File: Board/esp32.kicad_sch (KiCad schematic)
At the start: 7 parts, among them U1 ESP32-WROOM-32

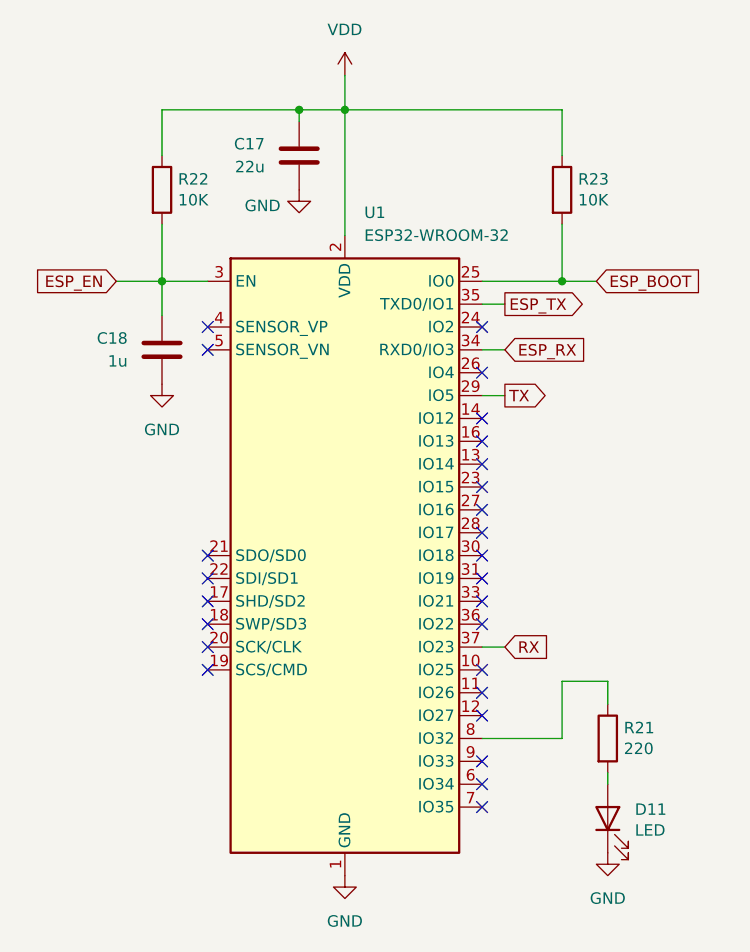
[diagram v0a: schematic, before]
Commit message: Minor fixes and improvements. Changes board shape.
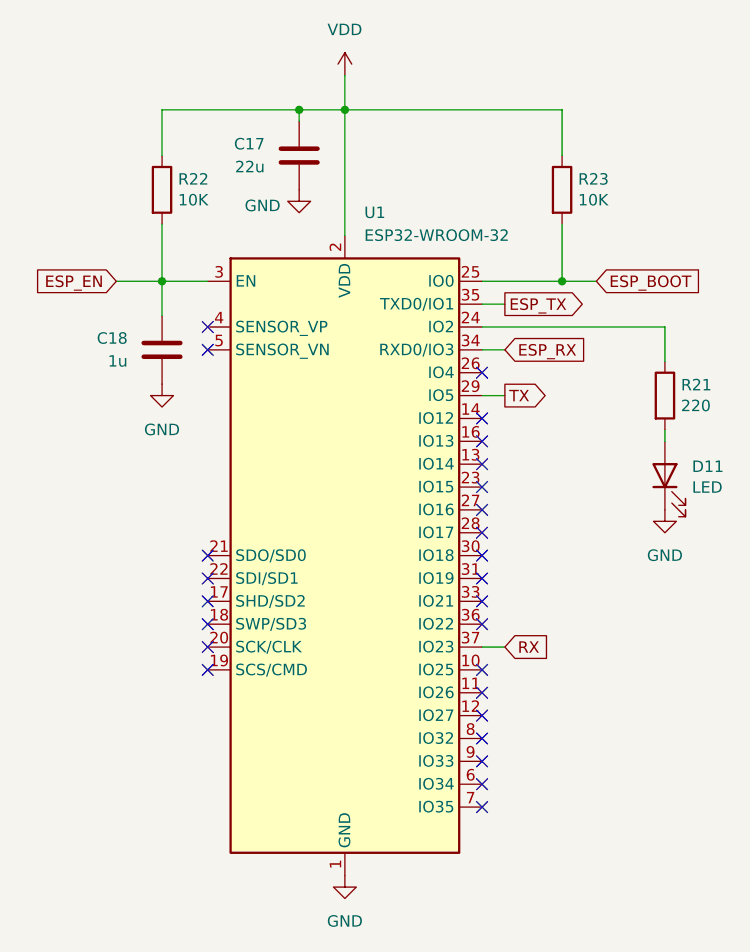
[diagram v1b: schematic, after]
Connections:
- net at R21.1: now also U1.24 (IO2); no longer U1.8 (IO32)
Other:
- moved on the sheet: D11, R21
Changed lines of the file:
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@@
 	)
 	(no_connect
-		(at 149.86 76.2)
+		(at 149.86 121.92)
 	)
 	(no_connect
@@
 	(wire
 		(pts
-			(xy 158.75 115.57) (xy 163.83 115.57)
+			(xy 170.18 76.2) (xy 170.18 80.01)
 		)
 		(stroke
@@
 	(wire
 		(pts
-			(xy 163.83 115.57) (xy 163.83 118.11)
+			(xy 170.18 76.2) (xy 149.86 76.2)
 		)
 		(stroke
@@
 	(wire
 		(pts
-			(xy 149.86 121.92) (xy 158.75 121.92)
-		)
-		(stroke
-			(width 0)
-			(type default)
-		)
-	)
-	(wire
-		(pts
 			(xy 162.56 71.12) (xy 158.75 71.12)
 		)
@@
 	(wire
 		(pts
-			(xy 158.75 121.92) (xy 158.75 115.57)
-		)
-		(stroke
-			(width 0)
-			(type default)
-		)
-	)
-	(wire
-		(pts
 			(xy 114.3 71.12) (xy 119.38 71.12)
 		)
@@
 	(wire
 		(pts
-			(xy 163.83 125.73) (xy 163.83 127)
+			(xy 170.18 87.63) (xy 170.18 88.9)
 		)
 		(stroke
@@
 	(symbol
 		(lib_id "Device:R")
-		(at 163.83 121.92 0)
+		(at 170.18 83.82 0)
 		(unit 1)
 		(exclude_from_sim no)
@@
 		(dnp no)
 		(property "Reference" "R21"
-			(at 165.608 120.7516 0)
+			(at 171.958 82.6516 0)
 			(effects
 				(font
@@
 		)
 		(property "Value" "220"
-			(at 165.608 123.063 0)
+			(at 171.958 84.963 0)
 			(effects
 				(font
@@
 		)
 		(property "Footprint" "Resistor_SMD:R_0805_2012Metric"
-			(at 162.052 121.92 90)
+			(at 168.402 83.82 90)
 			(effects
 				(font
@@
 		)
 		(property "Datasheet" "~"
-			(at 163.83 121.92 0)
+			(at 170.18 83.82 0)
 			(effects
 				(font
@@
 		)
 		(property "Description" ""
-			(at 163.83 121.92 0)
+			(at 170.18 83.82 0)
 			(effects
 				(font
@@
 	(symbol
 		(lib_id "power:GND")
-		(at 163.83 134.62 0)
+		(at 170.18 96.52 0)
 		(unit 1)
 		(exclude_from_sim no)
@@
 		(fields_autoplaced yes)
 		(property "Reference" "#PWR033"
-			(at 163.83 140.97 0)
+			(at 170.18 102.87 0)
 			(effects
 				(font
@@
 		)
 		(property "Value" "GND"
-			(at 163.83 139.7 0)
+			(at 170.18 101.6 0)
 			(effects
 				(font
@@
 		)
 		(property "Footprint" ""
-			(at 163.83 134.62 0)
+			(at 170.18 96.52 0)
 			(effects
 				(font
@@
 		)
 		(property "Datasheet" ""
-			(at 163.83 134.62 0)
+			(at 170.18 96.52 0)
 			(effects
 				(font
@@
 		)
 		(property "Description" "Power symbol creates a global label with name \"GND\" , ground"
-			(at 163.83 134.62 0)
+			(at 170.18 96.52 0)
 			(effects
 				(font
@@
 	(symbol
 		(lib_id "Device:LED")
-		(at 163.83 130.81 90)
+		(at 170.18 92.71 90)
 		(unit 1)
 		(exclude_from_sim no)
@@
 		(dnp no)
 		(property "Reference" "D11"
-			(at 166.8272 129.8194 90)
+			(at 173.1772 91.7194 90)
 			(effects
 				(font
@@
 		)
 		(property "Value" "LED"
-			(at 166.8272 132.1308 90)
+			(at 173.1772 94.0308 90)
 			(effects
 				(font
@@
 		)
 		(property "Footprint" "LED_SMD:LED_0805_2012Metric"
-			(at 163.83 130.81 0)
+			(at 170.18 92.71 0)
 			(effects
 				(font
@@
 		)
 		(property "Datasheet" "~"
-			(at 163.83 130.81 0)
-			(effects
-				(font
-					(size 1.27 1.27)
-				)
-				(hide yes)
-			)
-		)
-		(property "Description" ""
-			(at 163.83 130.81 0)
-			(effects
-				(font
+			(at 170.18 92.71 0)
+			(effects
+				(font
+					(size 1.27 1.27)
+				)
+				(hide yes)
+			)
+		)
+		(property "Description" "Light emitting diode"
+			(at 170.18 92.71 0)
+			(effects
+				(font
+					(size 1.27 1.27)
+				)
+				(hide yes)
+			)
+		)
+		(property "Sim.Pins" "1=K 2=A"
+			(at 170.18 92.71 0)
+			(effects
+				(font

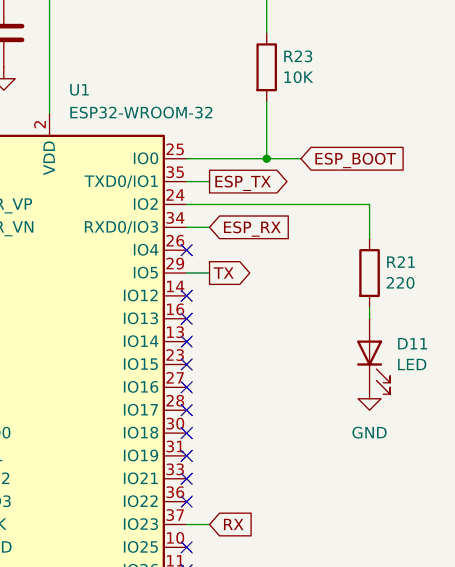
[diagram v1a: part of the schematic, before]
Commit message: Fixes constant current circuit.
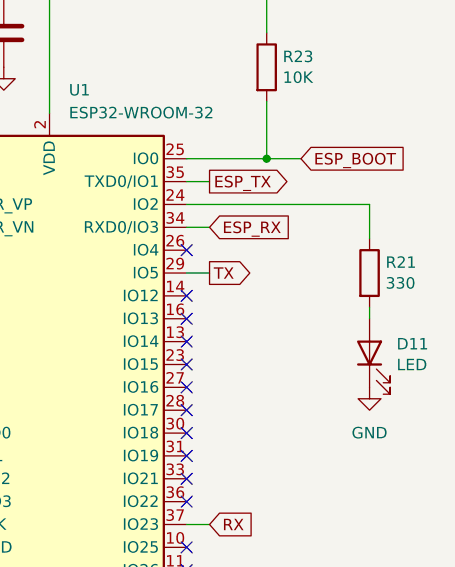
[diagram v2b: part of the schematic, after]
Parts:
- R21: value 220 -> 330
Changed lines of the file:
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@@
 			)
 		)
-		(property "Value" "220"
+		(property "Value" "330"
 			(at 171.958 84.963 0)
 			(effects
